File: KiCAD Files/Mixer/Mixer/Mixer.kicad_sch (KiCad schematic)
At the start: 64 parts, among them IC1 FST3253MTCX, K1 G6K-2F-Y DC3, U1 OPA1678IDGKT, U2 OPA1678IDGKT, U3 OPA1678IDGKT, U4 NC7SZ04P5X, U5 4053, U6 4053

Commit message: update only
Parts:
- removed IQ_Clk1: Conn_01x04_Socket, Connector_PinHeader_2.54mm:PinHeader_1x04_P2.54mm_Vertical, symbol Connector:Conn_01x04_Socket
- added IQ_Clock_in1: Conn_01x03_Socket, Connector_JST:JST_EH_B3B-EH-A_1x03_P2.50mm_Vertical, symbol Connector:Conn_01x03_Socket
- added JP1, JP2: SolderJumper_3_Open, Jumper:SolderJumper-3_P1.3mm_Open_Pad1.0x1.5mm_NumberLabels, symbol Jumper:SolderJumper_3_Open
- added R5, R8: 100R, Resistor_SMD:R_0805_2012Metric_Pad1.20x1.40mm_HandSolder, symbol Device:R
- added U2: SN74AC74PWR, Private:74AC74-L, symbol Private:SN74AC74PWR
- renumbered R8 to R10, R9 to R11, R10 to R12, R11 to R13, R12 to R14, R13 to R15, R14 to R16, R15 to R17, R16 to R18, R17 to R19, R18 to R20, R5 to R6, R6 to R7, R7 to R9, U2 to U3, U3 to U4, U4 to U5, U5 to U6, U6 to U7
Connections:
- net +5V: now also U2.1 (*1CLR), U2.10 (*2PRE), U2.13 (*2CLR), U2.14 (VCC), U2.4 (*1PRE)
- net Clk_S0: now also R8.1, U2.9 (2Q); no longer IC1.14 (S0)
- net Clk_S1: now also R5.1, U2.6 (*1Q); no longer IC1.2 (S1)
- net GND: now also IQ_Clock_in1.1 (Pin_1), IQ_Clock_in1.3 (Pin_3), U2.7 (GND)
- new net: JP1.2 (C), R5.2
- new net: IQ_Clock_in1.2 (Pin_2), U2.11 (2CLK), U2.3 (1CLK)
- new net: U2.12 (2D), U2.5 (1Q)
- new net: U2.2 (1D), U2.8 (*2Q)
- new net: JP2.2 (C), R8.2
- new net S0: IC1.14 (S0), JP1.1 (A), JP2.1 (A)
- new net S1: IC1.2 (S1), JP1.3 (B), JP2.3 (B)

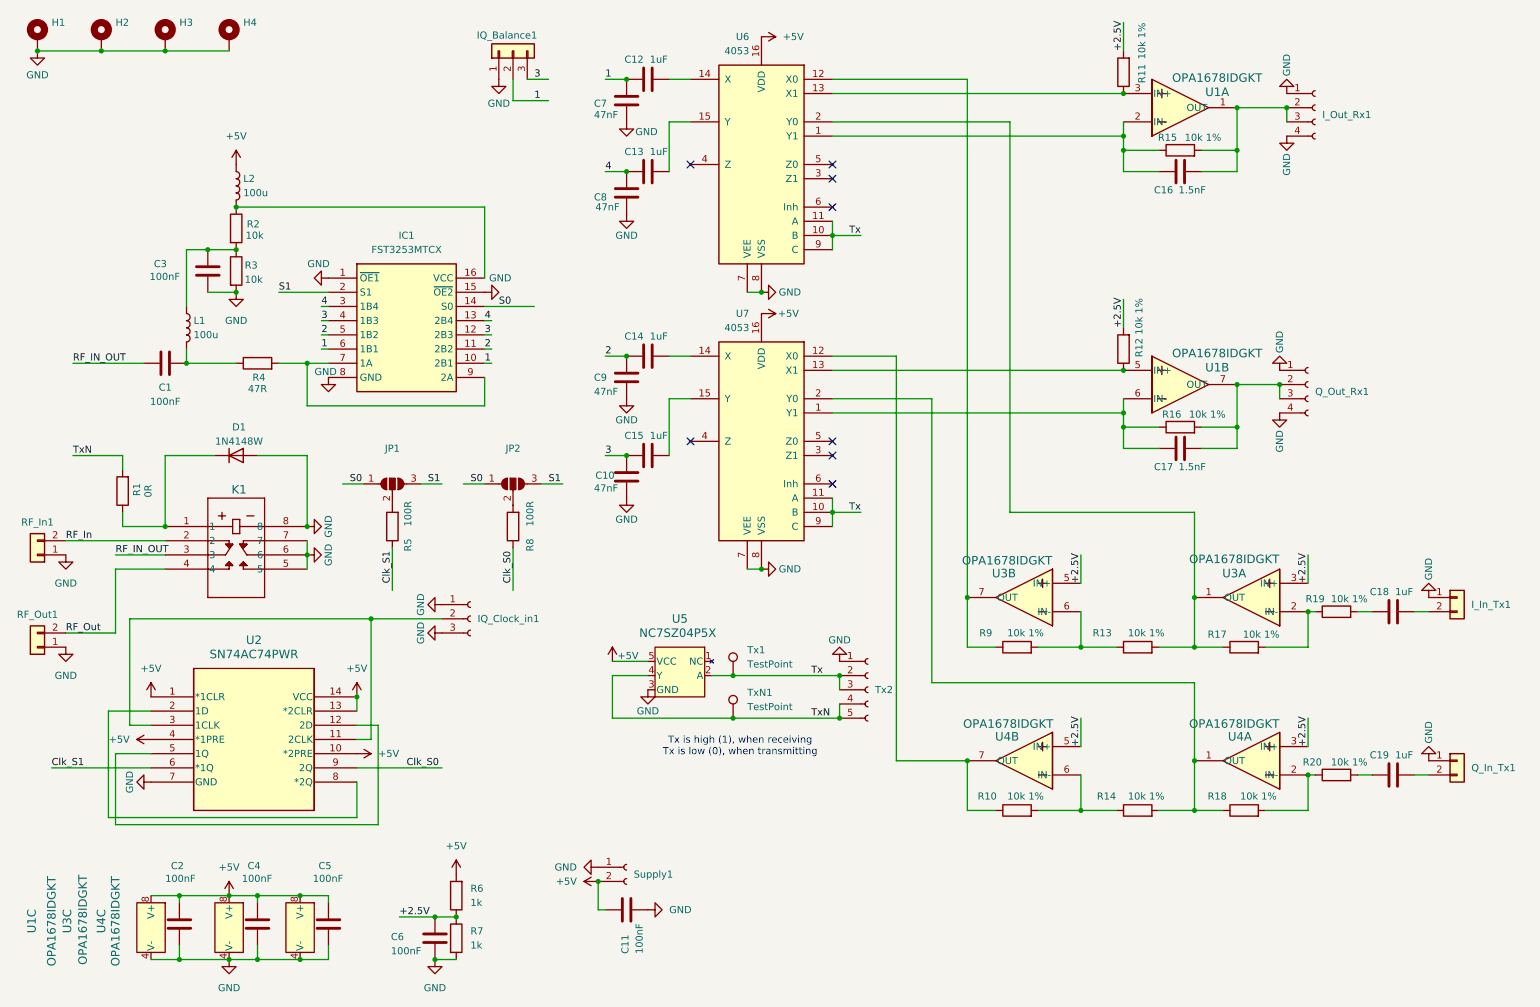
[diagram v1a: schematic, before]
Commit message: added 74AC74 at mixer board
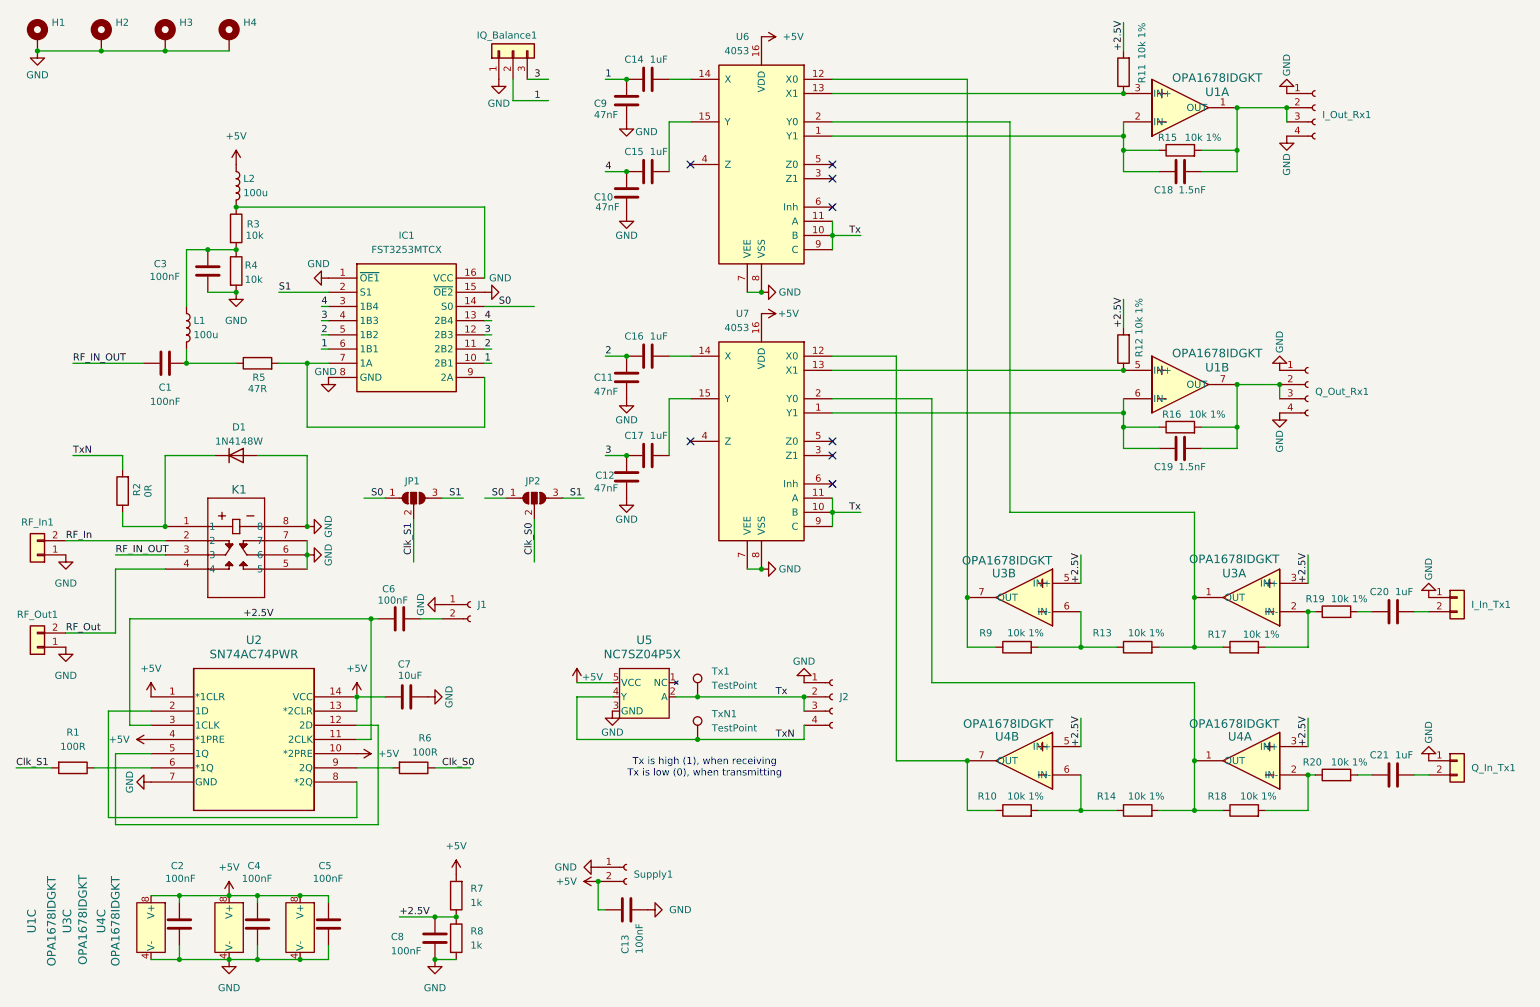
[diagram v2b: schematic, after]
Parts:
- removed IQ_Clock_in1: Conn_01x03_Socket, Connector_JST:JST_EH_B3B-EH-A_1x03_P2.50mm_Vertical, symbol Connector:Conn_01x03_Socket
- removed R5, R8: 100R, Resistor_SMD:R_0805_2012Metric_Pad1.20x1.40mm_HandSolder, symbol Device:R
- removed Tx2: Conn_01x05_Socket, Connector_JST:JST_EH_B5B-EH-A_1x05_P2.50mm_Vertical, symbol Connector:Conn_01x05_Socket
- added C6: 100nF, Capacitor_SMD:C_0805_2012Metric_Pad1.18x1.45mm_HandSolder, symbol Device:C
- added C7: 10uF, Capacitor_SMD:C_0805_2012Metric_Pad1.18x1.45mm_HandSolder, symbol Device:C
- added J1: Conn_01x02_Socket, Connector_JST:JST_EH_B2B-EH-A_1x02_P2.50mm_Vertical, symbol Connector:Conn_01x02_Socket
- added J2: Conn_01x04_Socket, Connector_JST:JST_EH_B4B-EH-A_1x04_P2.50mm_Vertical, symbol Connector:Conn_01x04_Socket
- added R1, R6: 100R, Resistor_SMD:R_0805_2012Metric_Pad1.20x1.40mm_HandSolder, symbol Device:R
- renumbered C8 to C10, C9 to C11, C10 to C12, C11 to C13, C12 to C14, C13 to C15, C14 to C16, C15 to C17, C16 to C18, C17 to C19, C18 to C20, C19 to C21, C6 to C8, C7 to C9, R1 to R2, R2 to R3, R3 to R4, R4 to R5, R6 to R7, R7 to R8
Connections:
- net +2.5V: now also U2.11 (2CLK), U2.3 (1CLK), C6.2
- net +5V: now also C7.2
- net Clk_S0: now also JP2.2 (C), R6.1; no longer U2.9 (2Q)
- net Clk_S1: now also JP1.2 (C), R1.2; no longer U2.6 (*1Q)
- net GND: now also C7.1, J1.1 (Pin_1), J2.1 (Pin_1)
- net Tx: now also J2.2 (Pin_2), J2.3 (Pin_3)
- net TxN: now also J2.4 (Pin_4)
- new net: R1.1, U2.6 (*1Q)
- new net: R6.2, U2.9 (2Q)
- new net: C6.1, J1.2 (Pin_2)
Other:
- moved on the sheet: JP1, JP2, Tx1, TxN1, U5

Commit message: more work on new Mixer
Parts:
- C6: footprint Capacitor_SMD:C_0805_2012Metric_Pad1.18x1.45mm_HandSolder -> Capacitor_SMD:C_0603_1608Metric_Pad1.08x0.95mm_HandSolder
- R1, R6: footprint Resistor_SMD:R_0805_2012Metric_Pad1.20x1.40mm_HandSolder -> Resistor_SMD:R_0603_1608Metric_Pad0.98x0.95mm_HandSolder
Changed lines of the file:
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@@
 		)
 	)
+	(label "S0"
+		(at 104.14 69.85 0)
+		(fields_autoplaced yes)
+		(effects
+			(font
+				(size 1.27 1.27)
+			)
+			(justify left bottom)
+		)
+	)
 	(label "Clk_S0"
 		(at 107.95 114.3 90)
@@
 		)
 	)
-	(label "S0"
-		(at 101.6 69.85 0)
-		(fields_autoplaced yes)
-		(effects
-			(font
-				(size 1.27 1.27)
-			)
-			(justify left bottom)
-		)
-	)
 	(label "3"
 		(at 107.95 29.21 0)
@@
 			)
 		)
-		(property "Footprint" "Resistor_SMD:R_0805_2012Metric_Pad1.20x1.40mm_HandSolder"
+		(property "Footprint" "Resistor_SMD:R_0603_1608Metric_Pad0.98x0.95mm_HandSolder"
 			(at 25.4 150.622 90)
 			(effects
@@
 			)
 		)
-		(property "Footprint" "Resistor_SMD:R_0805_2012Metric_Pad1.20x1.40mm_HandSolder"
+		(property "Footprint" "Resistor_SMD:R_0603_1608Metric_Pad0.98x0.95mm_HandSolder"
 			(at 86.36 150.622 90)
 			(effects
@@
 			)
 		)
-		(property "Footprint" "Capacitor_SMD:C_0805_2012Metric_Pad1.18x1.45mm_HandSolder"
+		(property "Footprint" "Capacitor_SMD:C_0603_1608Metric_Pad1.08x0.95mm_HandSolder"
 			(at 80.01 126.6952 0)
 			(effects

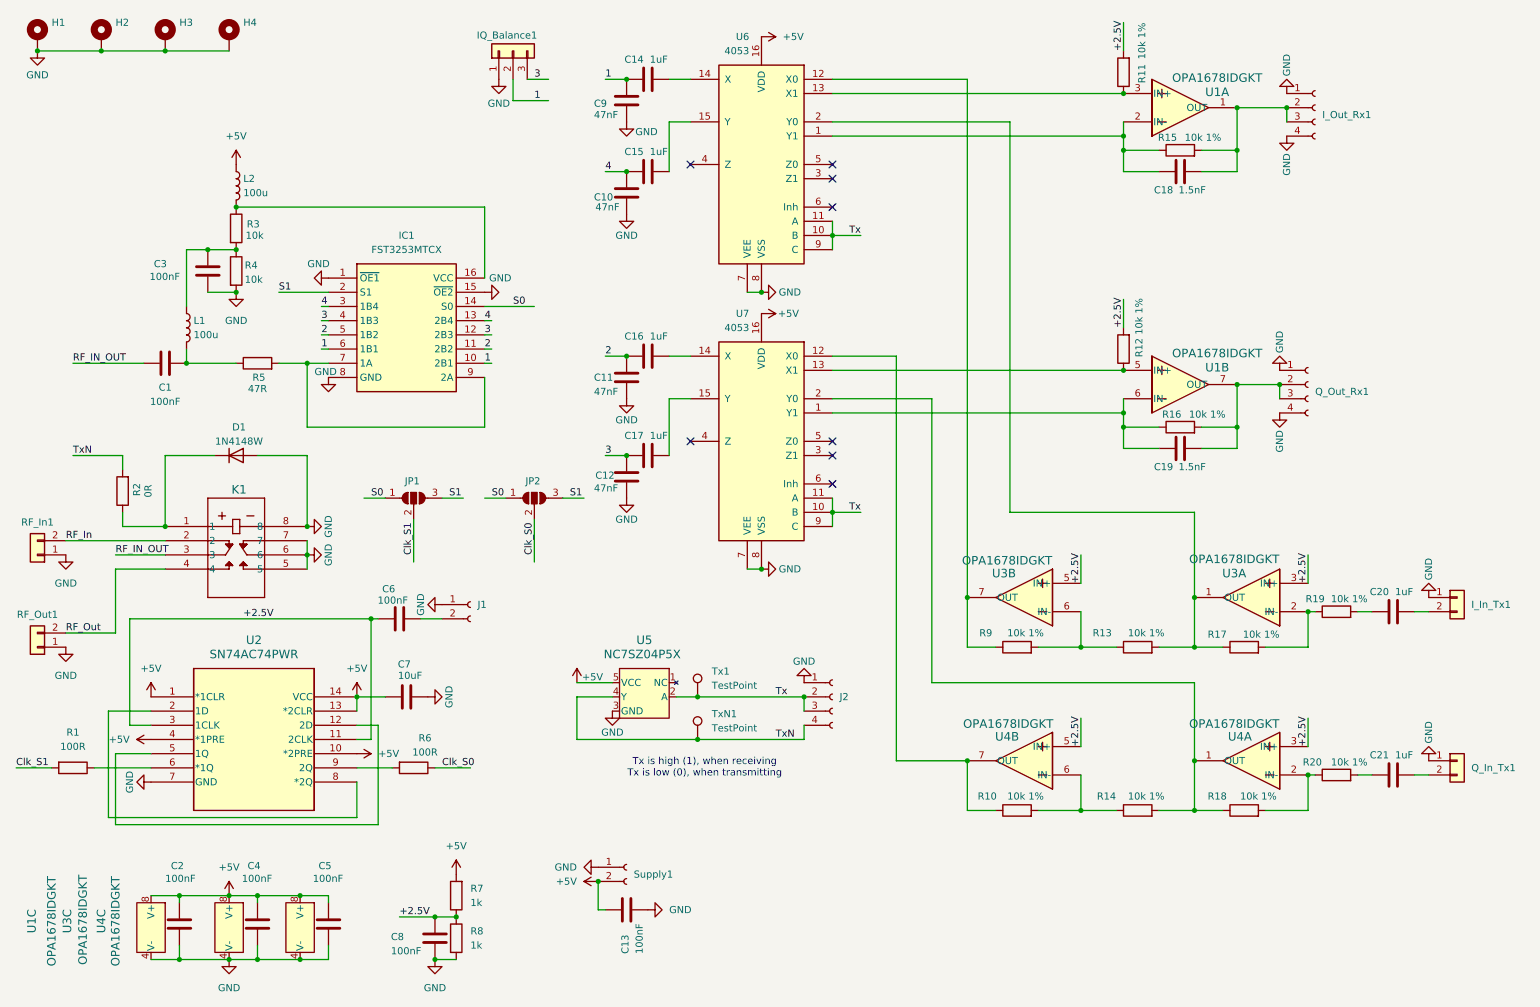
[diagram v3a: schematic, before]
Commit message: added ti mixer board
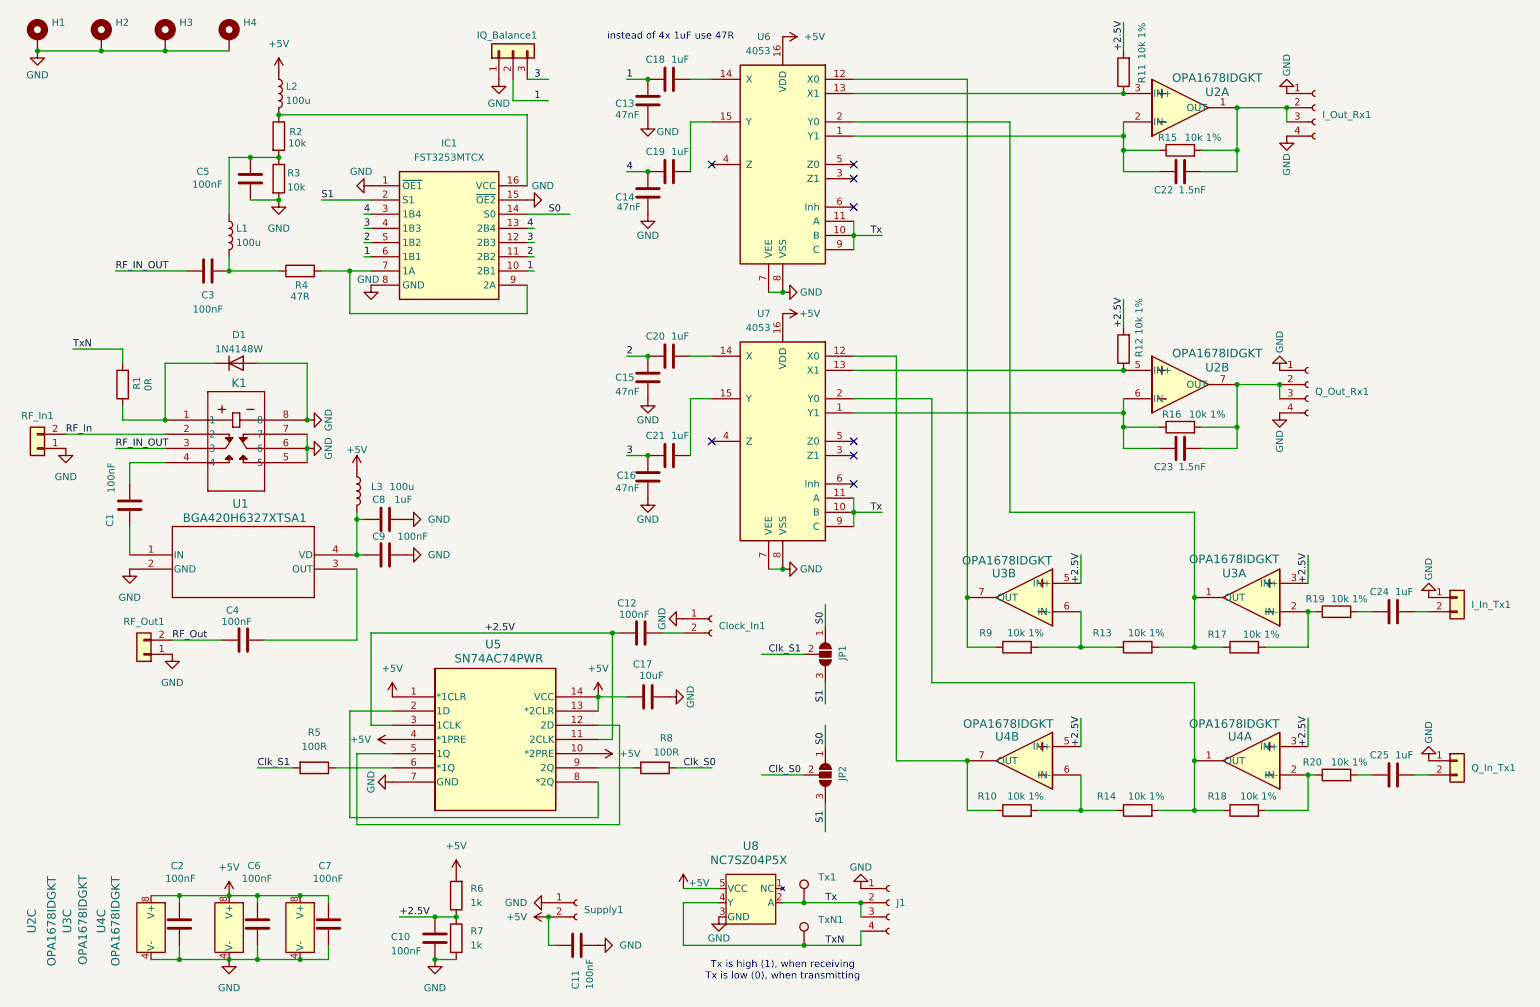
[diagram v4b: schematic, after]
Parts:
- added C1, C4, C9: 100nF, Capacitor_SMD:C_0603_1608Metric_Pad1.08x0.95mm_HandSolder, symbol Device:C
- added C8: 1uF, Capacitor_SMD:C_0805_2012Metric_Pad1.18x1.45mm_HandSolder, symbol Device:C
- added L3: 100u, Inductor_SMD:L_0805_2012Metric_Pad1.15x1.40mm_HandSolder, symbol Device:L
- added U1: BGA420H6327XTSA1, Private:PG-SOT343-4-1_INF, symbol Private:BGA420H6327XTSA1
- renumbered C8 to C10, C13 to C11, C6 to C12, C9 to C13, C10 to C14, C11 to C15, C12 to C16, C7 to C17, C14 to C18, C15 to C19, C16 to C20, C17 to C21, C18 to C22, C19 to C23, C20 to C24, C21 to C25, C1 to C3, C3 to C5, C4 to C6, C5 to C7, J1 to Clock_In1, J2 to J1, R2 to R1, R3 to R2, R4 to R3, R5 to R4, R1 to R5, R7 to R6, R8 to R7, R6 to R8, U1 to U2, U2 to U5, U5 to U8
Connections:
- net +5V: now also L3.1
- net GND: now also C8.1, C9.1, U1.2 (GND)
- net RF_Out: now also C4.2; no longer K1.4
- new net: C1.1, K1.4
- new net: C1.2, U1.1 (IN)
- new net: C8.2, C9.2, L3.2, U1.4 (VD)
- new net: C4.1, U1.3 (OUT)
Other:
- note added: "instead of 4x 1uF use 47R"
- moved on the sheet: C11, C12, C13, C14, C15, C16, C17, C18, C19, C20, C21, C3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
